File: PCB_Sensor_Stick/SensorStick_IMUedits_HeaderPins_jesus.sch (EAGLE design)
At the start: 48 parts, among them IC1 SAM-M8Q-0-10, IC2 STM32L412RBT6P, IC3 DPS310XTSA1, IC5 BMI085, IC6 IIS2MDCTR, J1 USB4160-03-0230-C, U1 4525DO-DS5AI001DP, U2 LD39050PU33R

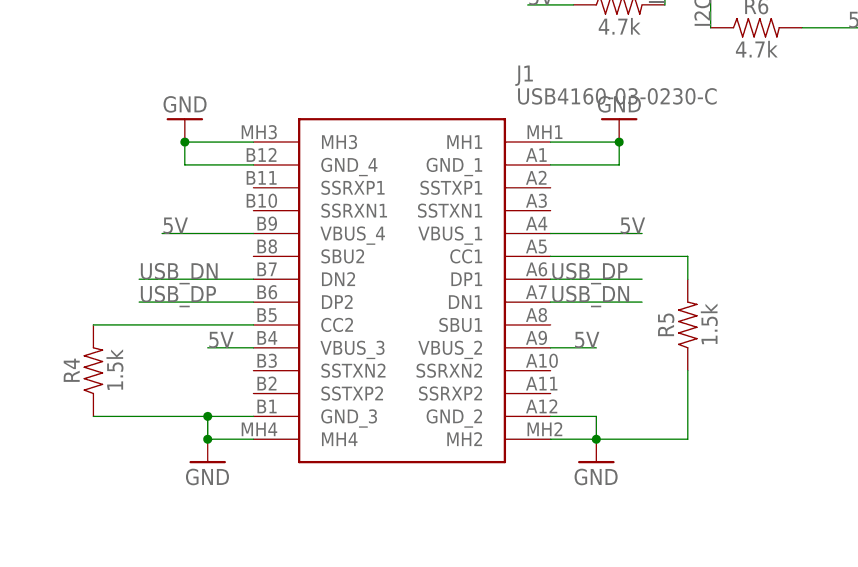
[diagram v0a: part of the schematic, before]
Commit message: J- Added power supply module to layout, missing USB-C
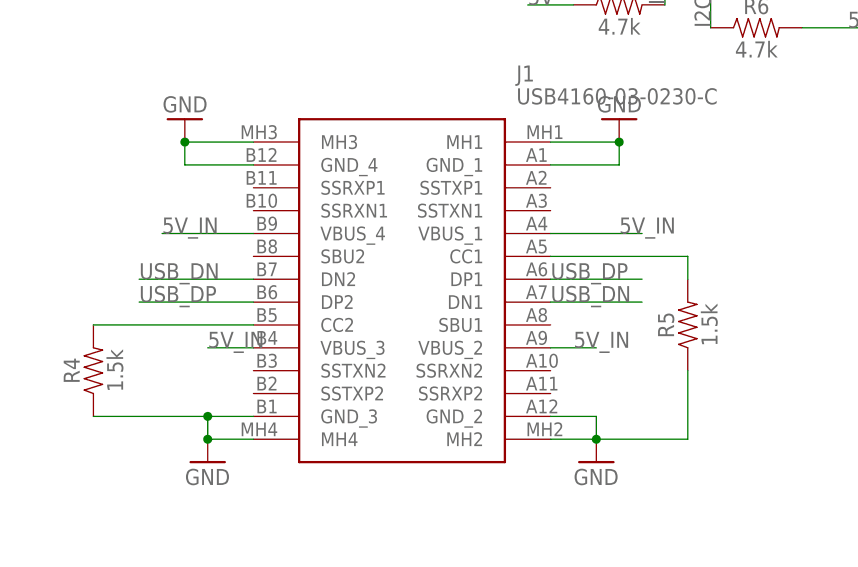
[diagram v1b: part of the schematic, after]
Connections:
- net 5V: no longer J1.VBUS_1, J1.VBUS_2, J1.VBUS_3, J1.VBUS_4
- net 5V_IN: now also J1.VBUS_1, J1.VBUS_2, J1.VBUS_3, J1.VBUS_4
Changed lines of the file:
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@@
-</segment>
-<segment>
-<pinref part="J1" gate="G$1" pin="VBUS_3"/>
-<wire x1="152.4" y1="-63.5" x2="147.32" y2="-63.5" width="0.1524" layer="91"/>
-<label x="147.32" y="-63.5" size="1.778" layer="95"/>
-</segment>
-<segment>
-<pinref part="J1" gate="G$1" pin="VBUS_2"/>
-<wire x1="185.42" y1="-63.5" x2="190.5" y2="-63.5" width="0.1524" layer="91"/>
-<label x="187.96" y="-63.5" size="1.778" layer="95"/>
-</segment>
-<segment>
-<pinref part="J1" gate="G$1" pin="VBUS_4"/>
-<wire x1="152.4" y1="-50.8" x2="142.24" y2="-50.8" width="0.1524" layer="91"/>
-<label x="142.24" y="-50.8" size="1.778" layer="95"/>
-</segment>
-<segment>
-<pinref part="J1" gate="G$1" pin="VBUS_1"/>
-<wire x1="185.42" y1="-50.8" x2="195.58" y2="-50.8" width="0.1524" layer="91"/>
-<label x="193.04" y="-50.8" size="1.778" layer="95"/>
 </segment>
 <segment>
@@
 <label x="-48.26" y="-33.02" size="1.778" layer="95"/>
 </segment>
+<segment>
+<pinref part="J1" gate="G$1" pin="VBUS_4"/>
+<wire x1="152.4" y1="-50.8" x2="142.24" y2="-50.8" width="0.1524" layer="91"/>
+<label x="142.24" y="-50.8" size="1.778" layer="95"/>
+</segment>
+<segment>
+<pinref part="J1" gate="G$1" pin="VBUS_1"/>
+<wire x1="185.42" y1="-50.8" x2="195.58" y2="-50.8" width="0.1524" layer="91"/>
+<label x="193.04" y="-50.8" size="1.778" layer="95"/>
+</segment>
+<segment>
+<pinref part="J1" gate="G$1" pin="VBUS_3"/>
+<wire x1="152.4" y1="-63.5" x2="147.32" y2="-63.5" width="0.1524" layer="91"/>
+<label x="147.32" y="-63.5" size="1.778" layer="95"/>
+</segment>
+<segment>
+<pinref part="J1" gate="G$1" pin="VBUS_2"/>
+<wire x1="185.42" y1="-63.5" x2="190.5" y2="-63.5" width="0.1524" layer="91"/>
+<label x="187.96" y="-63.5" size="1.778" layer="95"/>
+</segment>
 </net>

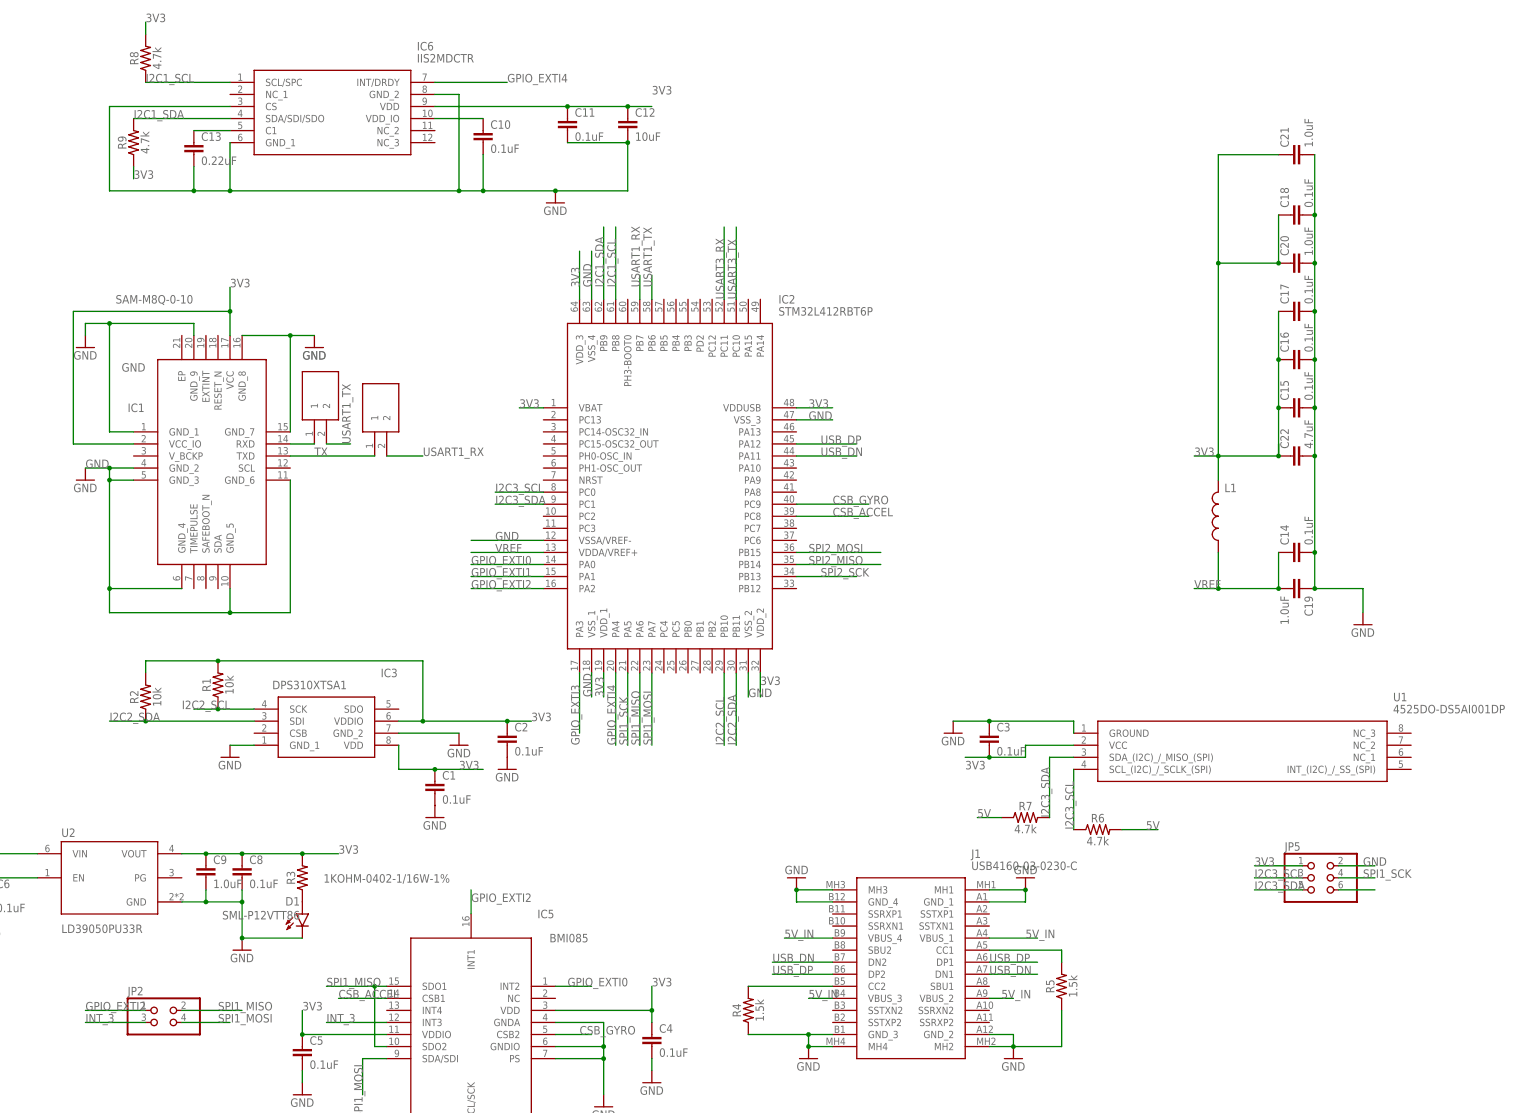
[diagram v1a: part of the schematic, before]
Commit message: J- Edited data ready lines and connections, Barometer missing
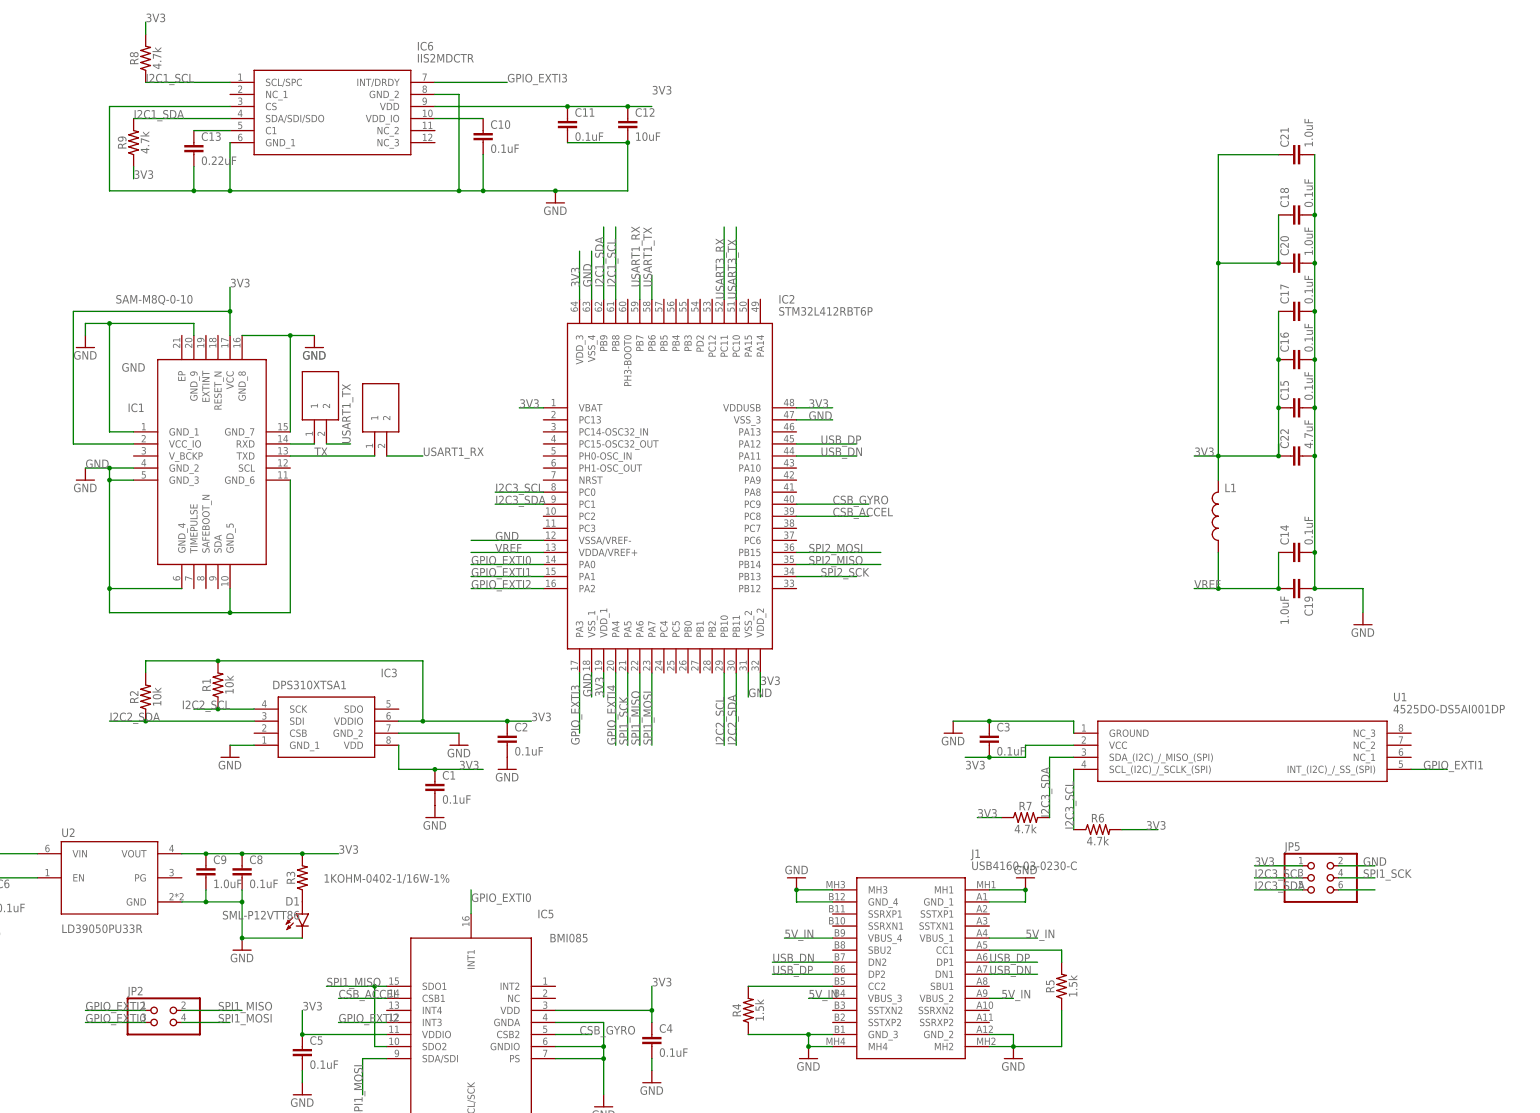
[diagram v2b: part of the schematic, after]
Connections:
- removed net INT_3: IC5.INT3, JP2.3
- net 3V3: now also R6.2, R7.1
- net 5V: no longer R6.2, R7.1
- net GPIO_EXTI0: now also IC5.INT1, JP2.3; no longer IC5.INT2
- net GPIO_EXTI1: now also U1.INT_(I2C)_/_SS_(SPI)
- net GPIO_EXTI2: now also IC5.INT3; no longer IC5.INT1
- net GPIO_EXTI3: now also IC6.INT/DRDY
- net GPIO_EXTI4: no longer IC6.INT/DRDY
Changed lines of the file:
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@@
 <label x="241.3" y="-35.56" size="1.778" layer="95"/>
+</segment>
+<segment>
+<pinref part="R6" gate="G$1" pin="2"/>
+<wire x1="213.36" y1="-27.94" x2="220.98" y2="-27.94" width="0.1524" layer="91"/>
+<label x="218.44" y="-27.94" size="1.778" layer="95"/>
+</segment>
+<segment>
+<pinref part="R7" gate="G$1" pin="1"/>
+<wire x1="187.96" y1="-25.4" x2="182.88" y2="-25.4" width="0.1524" layer="91"/>
+<label x="182.88" y="-25.4" size="1.778" layer="95"/>
 </segment>
 </net>
@@
 </segment>
 <segment>
-<pinref part="IC5" gate="G$1" pin="INT1"/>
-<wire x1="76.2" y1="-45.72" x2="76.2" y2="-40.64" width="0.1524" layer="91"/>
-<label x="76.2" y="-43.18" size="1.778" layer="95"/>
+<pinref part="IC5" gate="G$1" pin="INT3"/>
+<wire x1="58.42" y1="-68.58" x2="48.26" y2="-68.58" width="0.1524" layer="91"/>
+<label x="48.26" y="-68.58" size="1.778" layer="95"/>
 </segment>
 </net>
@@
 <label x="-25.4" y="-22.86" size="1.778" layer="95" rot="R180"/>
 </segment>
-<segment>
-<pinref part="R7" gate="G$1" pin="1"/>
-<wire x1="187.96" y1="-25.4" x2="182.88" y2="-25.4" width="0.1524" layer="91"/>
-<label x="182.88" y="-25.4" size="1.778" layer="95"/>
-</segment>
-<segment>
-<pinref part="R6" gate="G$1" pin="2"/>
-<wire x1="213.36" y1="-27.94" x2="220.98" y2="-27.94" width="0.1524" layer="91"/>
-<label x="218.44" y="-27.94" size="1.778" layer="95"/>
-</segment>
 </net>
 <net name="5V_IN" class="0">
@@
 <net name="GPIO_EXTI4" class="0">
 <segment>
+<pinref part="IC2" gate="G$1" pin="PA4"/>
+<wire x1="106.68" y1="5.08" x2="106.68" y2="-10.16" width="0.1524" layer="91"/>
+<label x="106.68" y="-10.16" size="1.778" layer="95" rot="R90"/>
+</segment>
+</net>
+<net name="USART3_RX" class="0">
+<segment>
+<pinref part="IC2" gate="G$1" pin="PC11"/>
+<wire x1="129.54" y1="83.82" x2="129.54" y2="99.06" width="0.1524" layer="91"/>
+<label x="129.54" y="83.82" size="1.778" layer="95" rot="R90"/>
+</segment>
+</net>
+<net name="USART3_TX" class="0">
+<segment>
+<pinref part="IC2" gate="G$1" pin="PC10"/>
+<wire x1="132.08" y1="83.82" x2="132.08" y2="99.06" width="0.1524" layer="91"/>
+<label x="132.08" y="83.82" size="1.778" layer="95" rot="R90"/>
+</segment>
+</net>
+<net name="SPI2_MOSI" class="0">
+<segment>
+<pinref part="IC2" gate="G$1" pin="PB15"/>
+<wire x1="144.78" y1="30.48" x2="162.56" y2="30.48" width="0.1524" layer="91"/>
+<label x="147.32" y="30.48" size="1.778" layer="95"/>
+</segment>
+<segment>
+<pinref part="JP4" gate="A" pin="5"/>
+<wire x1="-40.64" y1="88.9" x2="-53.34" y2="88.9" width="0.1524" layer="91"/>
+<label x="-53.34" y="88.9" size="1.778" layer="95"/>
+</segment>
+</net>
+<net name="SPI2_MISO" class="0">
+<segment>
+<pinref part="IC2" gate="G$1" pin="PB14"/>
+<wire x1="144.78" y1="27.94" x2="162.56" y2="27.94" width="0.1524" layer="91"/>
+<label x="147.32" y="27.94" size="1.778" layer="95"/>
+</segment>
+<segment>
+<pinref part="JP4" gate="A" pin="4"/>
+<wire x1="-40.64" y1="91.44" x2="-53.34" y2="91.44" width="0.1524" layer="91"/>
+<label x="-53.34" y="91.44" size="1.778" layer="95"/>
+</segment>
+</net>
+<net name="GPIO_EXTI0" class="0">
+<segment>
+<pinref part="IC2" gate="G$1" pin="PA0"/>
+<wire x1="91.44" y1="27.94" x2="76.2" y2="27.94" width="0.1524" layer="91"/>
+<label x="76.2" y="27.94" size="1.778" layer="95"/>
+</segment>
+<segment>
+<pinref part="IC5" gate="G$1" pin="INT1"/>
+<wire x1="76.2" y1="-45.72" x2="76.2" y2="-40.64" width="0.1524" layer="91"/>
+<label x="76.2" y="-43.18" size="1.778" layer="95"/>
+</segment>
+<segment>
+<pinref part="JP2" gate="A" pin="3"/>
+<wire x1="7.62" y1="-68.58" x2="-5.08" y2="-68.58" width="0.1524" layer="91"/>
+<label x="-5.08" y="-68.58" size="1.778" layer="95"/>
+</segment>
+</net>
+<net name="GPIO_EXTI1" class="0">
+<segment>
+<pinref part="IC2" gate="G$1" pin="PA1"/>
+<wire x1="91.44" y1="25.4" x2="76.2" y2="25.4" width="0.1524" layer="91"/>
+<label x="76.2" y="25.4" size="1.778" layer="95"/>
+</segment>
+<segment>
+<pinref part="U1" gate="G$1" pin="INT_(I2C)_/_SS_(SPI)"/>
+<wire x1="274.32" y1="-15.24" x2="281.94" y2="-15.24" width="0.1524" layer="91"/>
+<label x="276.86" y="-15.24" size="1.778" layer="95"/>
+</segment>
+</net>
+<net name="GPIO_EXTI3" class="0">
+<segment>
+<pinref part="IC2" gate="G$1" pin="PA3"/>
+<wire x1="99.06" y1="5.08" x2="99.06" y2="-7.62" width="0.1524" layer="91"/>
+<label x="99.06" y="-10.16" size="1.778" layer="95" rot="R90"/>
+</segment>
+<segment>
 <pinref part="IC6" gate="G$1" pin="INT/DRDY"/>
 <wire x1="68.58" y1="129.54" x2="83.82" y2="129.54" width="0.1524" layer="91"/>
 <label x="83.82" y="129.54" size="1.778" layer="95"/>
-</segment>
-<segment>
-<pinref part="IC2" gate="G$1" pin="PA4"/>
-<wire x1="106.68" y1="5.08" x2="106.68" y2="-10.16" width="0.1524" layer="91"/>
-<label x="106.68" y="-10.16" size="1.778" layer="95" rot="R90"/>
-</segment>
-</net>
-<net name="USART3_RX" class="0">
-<segment>
-<pinref part="IC2" gate="G$1" pin="PC11"/>
-<wire x1="129.54" y1="83.82" x2="129.54" y2="99.06" width="0.1524" layer="91"/>
-<label x="129.54" y="83.82" size="1.778" layer="95" rot="R90"/>
-</segment>
-</net>
-<net name="USART3_TX" class="0">
-<segment>
-<pinref part="IC2" gate="G$1" pin="PC10"/>
-<wire x1="132.08" y1="83.82" x2="132.08" y2="99.06" width="0.1524" layer="91"/>
-<label x="132.08" y="83.82" size="1.778" layer="95" rot="R90"/>
-</segment>
-</net>
-<net name="SPI2_MOSI" class="0">
-<segment>
-<pinref part="IC2" gate="G$1" pin="PB15"/>
-<wire x1="144.78" y1="30.48" x2="162.56" y2="30.48" width="0.1524" layer="91"/>
-<label x="147.32" y="30.48" size="1.778" layer="95"/>
-</segment>
-<segment>
-<pinref part="JP4" gate="A" pin="5"/>
-<wire x1="-40.64" y1="88.9" x2="-53.34" y2="88.9" width="0.1524" layer="91"/>
-<label x="-53.34" y="88.9" size="1.778" layer="95"/>
-</segment>
-</net>
-<net name="SPI2_MISO" class="0">
-<segment>
-<pinref part="IC2" gate="G$1" pin="PB14"/>
-<wire x1="144.78" y1="27.94" x2="162.56" y2="27.94" width="0.1524" layer="91"/>
-<label x="147.32" y="27.94" size="1.778" layer="95"/>
-</segment>
-<segment>
-<pinref part="JP4" gate="A" pin="4"/>
-<wire x1="-40.64" y1="91.44" x2="-53.34" y2="91.44" width="0.1524" layer="91"/>
-<label x="-53.34" y="91.44" size="1.778" layer="95"/>
-</segment>
-</net>
-<net name="GPIO_EXTI0" class="0">
-<segment>
-<pinref part="IC2" gate="G$1" pin="PA0"/>
-<wire x1="91.44" y1="27.94" x2="76.2" y2="27.94" width="0.1524" layer="91"/>
-<label x="76.2" y="27.94" size="1.778" layer="95"/>
-</segment>
-<segment>
-<pinref part="IC5" gate="G$1" pin="INT2"/>
-<wire x1="93.98" y1="-60.96" x2="101.6" y2="-60.96" width="0.1524" layer="91"/>
-<label x="96.52" y="-60.96" size="1.778" layer="95"/>
-</segment>
-</net>
-<net name="GPIO_EXTI1" class="0">
-<segment>
-<pinref part="IC2" gate="G$1" pin="PA1"/>
-<wire x1="91.44" y1="25.4" x2="76.2" y2="25.4" width="0.1524" layer="91"/>
-<label x="76.2" y="25.4" size="1.778" layer="95"/>
-</segment>
-</net>
-<net name="GPIO_EXTI3" class="0">
-<segment>
-<pinref part="IC2" gate="G$1" pin="PA3"/>
-<wire x1="99.06" y1="5.08" x2="99.06" y2="-7.62" width="0.1524" layer="91"/>
-<label x="99.06" y="-10.16" size="1.778" layer="95" rot="R90"/>
 </segment>
 </net>
@@
 </segment>
 </net>
-<net name="INT_3" class="0">
-<segment>
-<pinref part="JP2" gate="A" pin="3"/>
-<wire x1="7.62" y1="-68.58" x2="-5.08" y2="-68.58" width="0.1524" layer="91"/>
-<label x="-5.08" y="-68.58" size="1.778" layer="95"/>
-</segment>
-<segment>
-<pinref part="IC5" gate="G$1" pin="INT3"/>
-<wire x1="45.72" y1="-68.58" x2="58.42" y2="-68.58" width="0.1524" layer="91"/>
-<label x="45.72" y="-68.58" size="1.778" layer="95"/>
-</segment>
-</net>

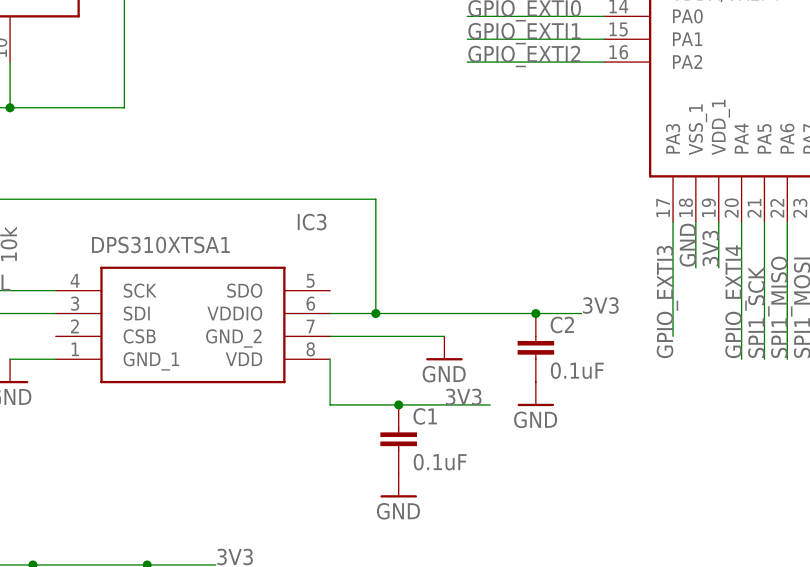
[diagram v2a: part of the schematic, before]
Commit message: J- Connected interrupt line for barometer
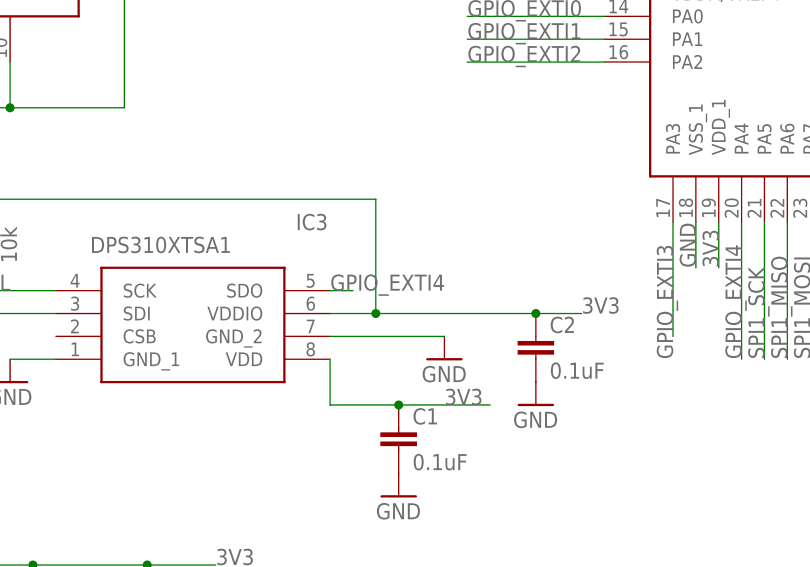
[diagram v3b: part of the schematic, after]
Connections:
- net GPIO_EXTI4: now also IC3.SDO
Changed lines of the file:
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@@
 <label x="106.68" y="-10.16" size="1.778" layer="95" rot="R90"/>
+</segment>
+<segment>
+<pinref part="IC3" gate="G$1" pin="SDO"/>
+<wire x1="60.96" y1="-2.54" x2="63.5" y2="-2.54" width="0.1524" layer="91"/>
+<label x="60.96" y="-2.54" size="1.778" layer="95"/>
 </segment>
 </net>
